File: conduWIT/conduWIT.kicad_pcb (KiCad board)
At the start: 2 copper layers, 68.6 x 53.3 mm, 8 parts, among them P1 Power, P2 Analog, P3 Digital, P4 Digital, P5 CONN_01X01, P6 CONN_01X01, P7 CONN_01X01, P8 CONN_01X01

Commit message: Made schematic and layout
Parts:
- added D1: LED, conduWIT_parts:LED_D5.0mm, F.Cu at (124.2, 112.0)
- added D2: LED, conduWIT_parts:LED_D5.0mm, F.Cu at (126.7, 99.3)
- added D3: LED, conduWIT_parts:LED_D5.0mm, F.Cu at (126.7, 84.1)
- added J10: SJ1-2503A, conduWIT_parts:CUI_SJ1-2503A, F.Cu at (114.0, 84.1)
- added J5: SJ1-2503A, conduWIT_parts:CUI_SJ1-2503A, F.Cu at (177.5, 112.0)
- added J6: SJ1-2503A, conduWIT_parts:CUI_SJ1-2503A, F.Cu at (177.5, 99.3)
- added J7: SJ1-2503A, conduWIT_parts:CUI_SJ1-2503A, F.Cu at (177.5, 84.1)
- added J8: SJ1-2503A, conduWIT_parts:CUI_SJ1-2503A, F.Cu at (114.0, 112.0)
- added J9: SJ1-2503A, conduWIT_parts:CUI_SJ1-2503A, F.Cu at (114.0, 99.3)
- added Q1: PN2222A, conduWIT_parts:TO-92_Inline, F.Cu at (164.8, 113.3)
- added Q2: PN2222A, conduWIT_parts:TO-92_Inline, F.Cu at (164.8, 101.8)
- added Q3: PN2222A, conduWIT_parts:TO-92_Inline, F.Cu at (164.8, 86.6)
- added R1: 10KΩ, conduWIT_parts:R_Axial_DIN0207_L6.3mm_D2.5mm_P7.62mm_Horizontal, F.Cu at (131.8, 117.1)
- added R2: 10KΩ, conduWIT_parts:R_Axial_DIN0207_L6.3mm_D2.5mm_P7.62mm_Horizontal, F.Cu at (131.8, 104.4)
- added R3: 10KΩ, conduWIT_parts:R_Axial_DIN0207_L6.3mm_D2.5mm_P7.62mm_Horizontal, F.Cu at (131.8, 81.5)
- added R4: 30Ω, conduWIT_parts:R_Axial_DIN0207_L6.3mm_D2.5mm_P7.62mm_Horizontal, F.Cu at (116.5, 119.6)
- added R5: 30Ω, conduWIT_parts:R_Axial_DIN0207_L6.3mm_D2.5mm_P7.62mm_Horizontal, F.Cu at (117.8, 105.7)
- added R6: 30Ω, conduWIT_parts:R_Axial_DIN0207_L6.3mm_D2.5mm_P7.62mm_Horizontal, F.Cu at (117.8, 90.4)
- J1: renamed from P3; value Digital -> Conn_01x10
- J2: renamed from P1; value Power -> Conn_01x08
- J3: renamed from P4; value Digital -> Conn_01x08
- J4: renamed from P2; value Analog -> Conn_01x06
- renumbered P5 to P1, P6 to P2, P7 to P3, P8 to P4
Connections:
- J2 pad 5: (no net) -> +5V
- J3 pad 1: (no net) -> 7
- J3 pad 2: (no net) -> 6(**)
- J3 pad 3: (no net) -> 5(**)
- J3 pad 4: (no net) -> 4
- J3 pad 5: (no net) -> 3(**)
- J3 pad 6: (no net) -> 2
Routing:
- net 5(**): track 0.00 -> 59.3 mm
- net 6(**): track 0.00 -> 48.9 mm
- net 7: track 0.00 -> 46.7 mm
- net 4: track 0.00 -> 38.5 mm
- net 3(**): track 0.00 -> 27.9 mm
- net Net-(J6-Pad1): track 0.00 -> 15.8 mm
- net Net-(J5-Pad1): track 0.00 -> 14.9 mm
- net Net-(J7-Pad1): track 0.00 -> 14.7 mm
- net 2: track 0.00 -> 12.8 mm
- net Net-(D1-Pad1): track 0.00 -> 7.62 mm
- net Net-(D2-Pad1): track 0.00 -> 7.55 mm
- net Net-(D3-Pad1): track 0.00 -> 6.88 mm
- added copper zone on B.Cu, net +5V
- removed copper zone on B.Cu, net GND
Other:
- outline, holes or cut-outs redrawn

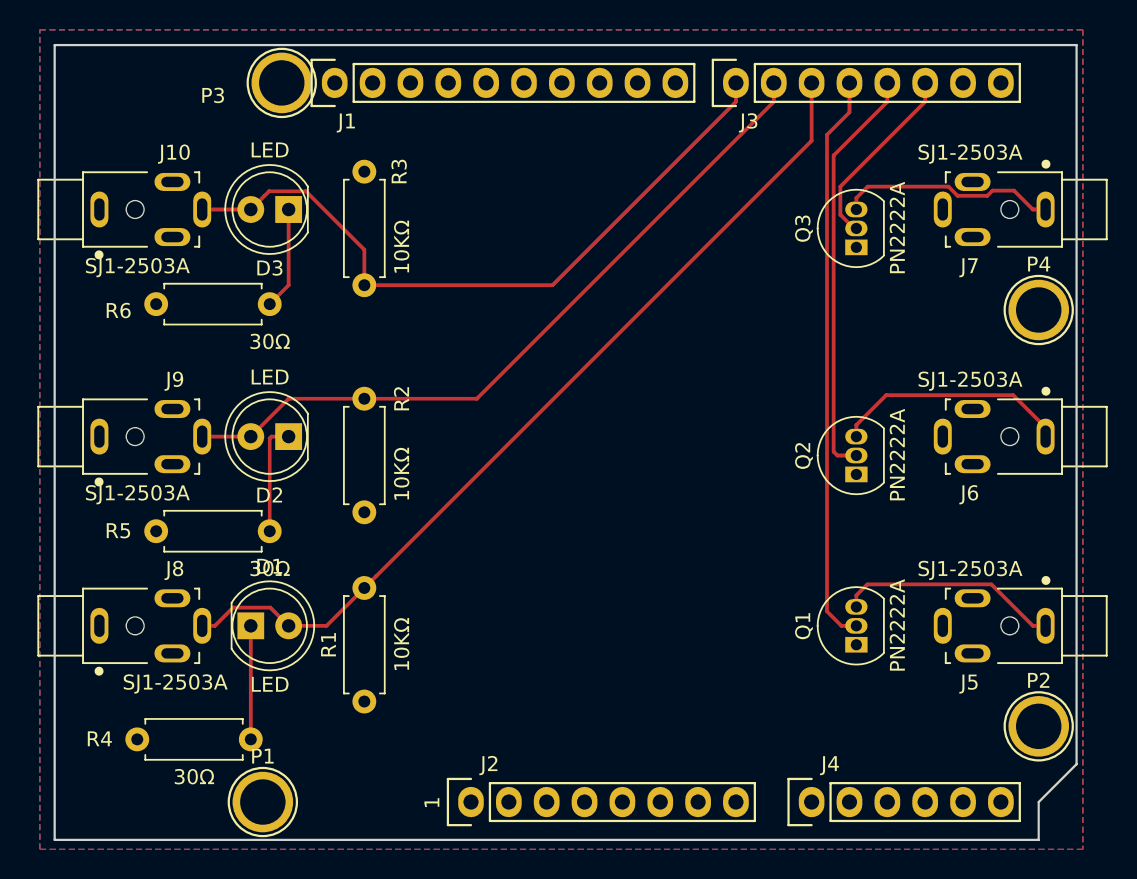
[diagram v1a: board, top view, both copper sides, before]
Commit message: Cleaned up layout
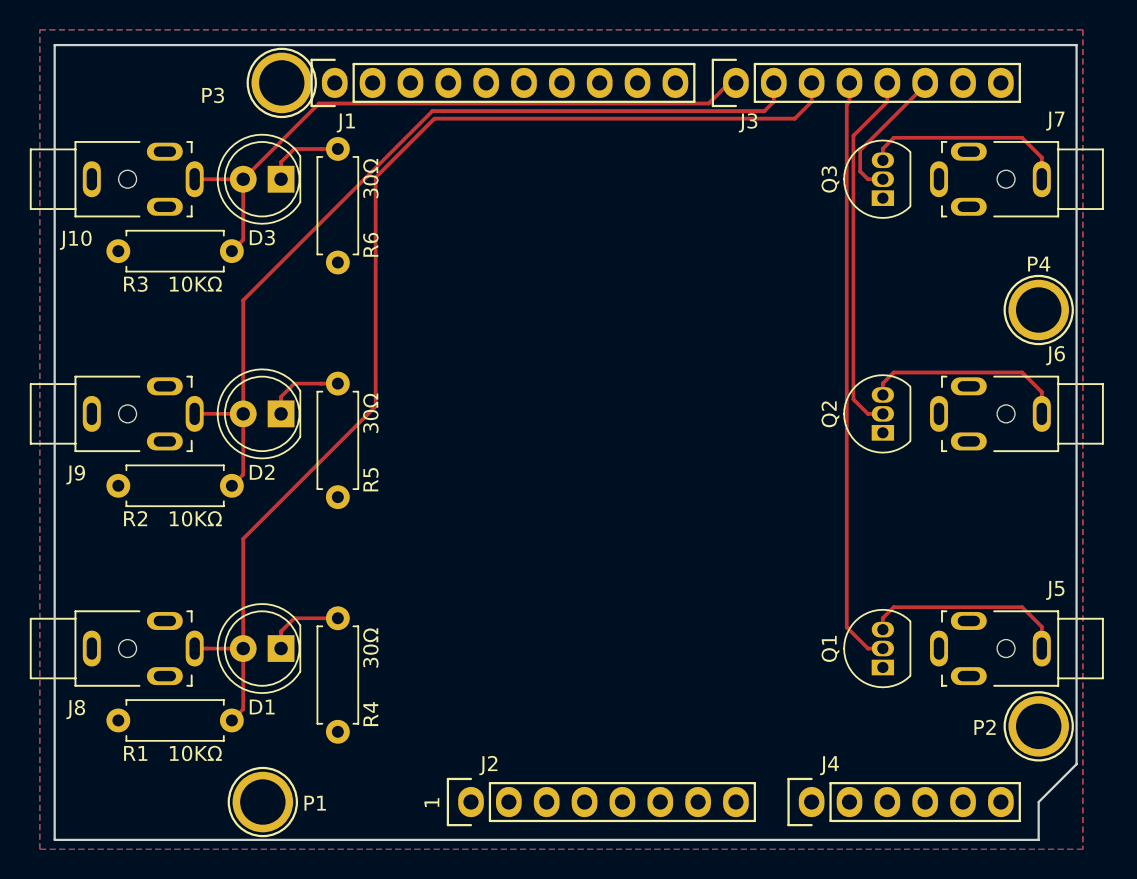
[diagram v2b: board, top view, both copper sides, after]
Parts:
- moved R3 17.4 mm to (115.3, 86.9), turned to 0 degrees
- moved R2 16.6 mm to (115.3, 102.6), turned to 0 degrees
- moved R1 16.6 mm to (115.3, 118.3), turned to 0 degrees
- moved R4 13.5 mm to (130.0, 119.1), turned to 90 degrees
- moved R6 12.5 mm to (130.0, 87.6), turned to 90 degrees
- moved R5 12.4 mm to (130.0, 103.4), turned to 90 degrees
- moved Q3 3.75 mm to (166.6, 83.3)
- moved Q2 3.31 mm to (166.6, 99.0)
- moved D1 2.54 mm to (126.2, 113.5), turned to 180 degrees
- moved Q1 2.34 mm to (166.6, 114.8)
- moved D3 2.09 mm to (126.2, 82.0)
- moved J10 2.09 mm to (113.5, 82.0)
- moved J7 2.05 mm to (177.2, 82.0)
- moved D2 1.61 mm to (126.2, 97.8)
- moved J8 1.61 mm to (113.5, 113.5)
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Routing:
- net 5(**): track 59.3 -> 76.3 mm
- net 6(**): track 48.9 -> 58.4 mm
- net 2: track 12.8 -> 9.49 mm
- net 3(**): track 27.9 -> 24.6 mm
- net 7: track 46.7 -> 44.3 mm
- net Net-(D1-Pad1): track 7.62 -> 5.33 mm
- net Net-(D2-Pad1): track 7.55 -> 5.33 mm
- net Net-(J6-Pad1): track 15.8 -> 13.8 mm
- net Net-(D3-Pad1): track 6.88 -> 5.33 mm
- net Net-(J5-Pad1): track 14.9 -> 13.8 mm
- net 4: track 38.5 -> 39.6 mm
- net Net-(J7-Pad1): track 14.7 -> 13.8 mm

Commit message: Art! Also cleaned up layout
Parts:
- added Ref**: Val**, conduWIT_parts:majora, F.Cu at (148.2, 98.9)

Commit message: Added ADC logo
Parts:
- removed the Ref** at (148.2, 98.9)
- added Ref**: Val**, conduWIT_parts:adc, F.Cu at (148.3, 99.3)

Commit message: Added signatures Added name, version, date
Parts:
- added Ref**: Val**, conduWIT_parts:signatures, B.Cu at (148.3, 99.3)
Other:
- board text added: "conduWIT 1.0.0 (03/2020)"

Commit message: Increased track width and clearance
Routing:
- net 6(**): track 58.4 -> 62.1 mm
- net 5(**): track 76.3 -> 80.0 mm
- net 3(**): track 24.6 -> 23.8 mm
- net 2: track 9.49 -> 8.73 mm
- net Net-(D1-Pad1): track 5.33 -> 4.65 mm
- net Net-(D3-Pad1): track 5.33 -> 4.65 mm
- net Net-(D2-Pad1): track 5.33 -> 4.65 mm
- net 7: track 44.3 -> 44.9 mm
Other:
- net class Default: clearance 0.2 -> 0.19558; trace_width 0.25 -> 0.3048; via_dia 0.6 -> 0.5842; via_drill 0.4 -> 0.3302
- rule trace_clearance: 0.2 -> 0.19558
- rule trace_min: 0.2 -> 0.3048
- rule via_min_drill: 0.3 -> 0.3302
- rule via_min_size: 0.4 -> 0.5842

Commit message: Final silkscreen touch-up
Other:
- board text added: "conduWIT 1.0.0 03/2020"
- board text removed: "conduWIT 1.0.0 (03/2020)"
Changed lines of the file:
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@@
     (visible_elements 7FFFFFFF)
     (pcbplotparams
-      (layerselection 0x00030_80000001)
-      (usegerberextensions false)
+      (layerselection 0x010f0_ffffffff)
+      (usegerberextensions true)
       (usegerberattributes false)
       (usegerberadvancedattributes false)
@@
       (outputformat 1)
       (mirror false)
-      (drillshape 1)
+      (drillshape 0)
       (scaleselection 1)
-      (outputdirectory ""))
+      (outputdirectory "mfg"))
   )
   (net 0 "")
@@
     (pad 1 thru_hole circle (at 0 0) (size 4.064 4.064) (drill 3.048) (layers *.Cu *.Mask F.SilkS))
   )
-  (gr_text "conduWIT 1.0.0 (03/2020)" (at 160.736 118.985 180) (layer B.SilkS)
-    (effects (font (size 1.25 1.25) (thickness 0.28)) (justify mirror))
+  (gr_text "conduWIT\n1.0.0\n03/2020" (at 167.467 119.239 180) (layer B.SilkS)
+    (effects (font (size 1 1) (thickness 0.15)) (justify mirror))
   )
   (gr_text 1 (at 136.352 123.8745 90) (layer F.SilkS)

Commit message: Updated resistor values on ConduWIT
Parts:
- R1, R2, R3: value 10KΩ -> 5.1KΩ
- R4, R5, R6: value 30Ω -> 150Ω
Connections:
- J1 pad 1: (no net) -> unconnected-(J1-Pad1)
- J1 pad 10: (no net) -> 8
- J1 pad 2: (no net) -> unconnected-(J1-Pad2)
- J1 pad 3: (no net) -> AREF
- J1 pad 5: (no net) -> 13(SCK)
- J1 pad 6: (no net) -> 12(MISO)
- J1 pad 7: (no net) -> 11(**/MOSI)
- J1 pad 8: (no net) -> 10(**/SS)
- J1 pad 9: (no net) -> 9(**)
- J2 pad 1: (no net) -> unconnected-(J2-Pad1)
- J2 pad 2: (no net) -> IOREF
- J2 pad 3: (no net) -> Reset
- J2 pad 4: (no net) -> +3.3V
- J2 pad 8: (no net) -> Vin
- J3 pad 7: (no net) -> 1(Tx)
- J3 pad 8: (no net) -> 0(Rx)
- J4 pad 1: (no net) -> A0
- J4 pad 2: (no net) -> A1
- J4 pad 3: (no net) -> A2
- J4 pad 4: (no net) -> A3
- J4 pad 5: (no net) -> A4(SDA)
- J4 pad 6: (no net) -> A5(SCL)
- J5 pad 4: (no net) -> unconnected-(J5-Pad4)
- J6 pad 4: (no net) -> unconnected-(J6-Pad4)
- J7 pad 4: (no net) -> unconnected-(J7-Pad4)
- P1 pad 1: (no net) -> unconnected-(P1-Pad1)
- P2 pad 1: (no net) -> unconnected-(P2-Pad1)
- P3 pad 1: (no net) -> unconnected-(P3-Pad1)
- P4 pad 1: (no net) -> unconnected-(P4-Pad1)
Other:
- net class Default removed
- board text added: "conduWIT 1.0.1 01/2023"
- board text removed: "conduWIT 1.0.0 03/2020"
